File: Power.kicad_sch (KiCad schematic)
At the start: 26 parts, among them J401 KLDX-0202-B, J402 EBWA-02-B, Q401 MCU18P10Y-TP, U401 TPS7A2030PDBVR

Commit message: feat: checked REV A
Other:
- moved on the sheet: C404, C405, FID401, FID402, FID403, H401, H402, H403, H404, ID401, TP403, TP404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

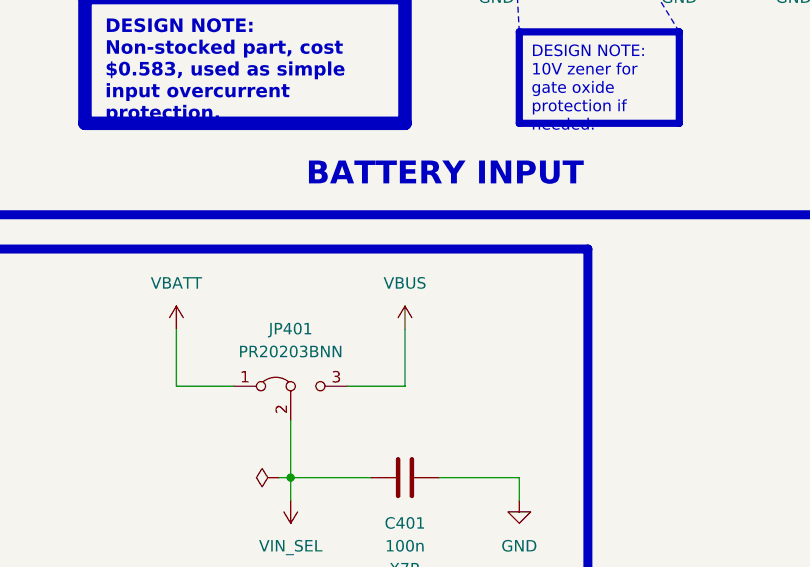
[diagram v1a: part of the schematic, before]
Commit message: fix: net naming, NC STM32 pins, silkscreen, pin 1 indicator
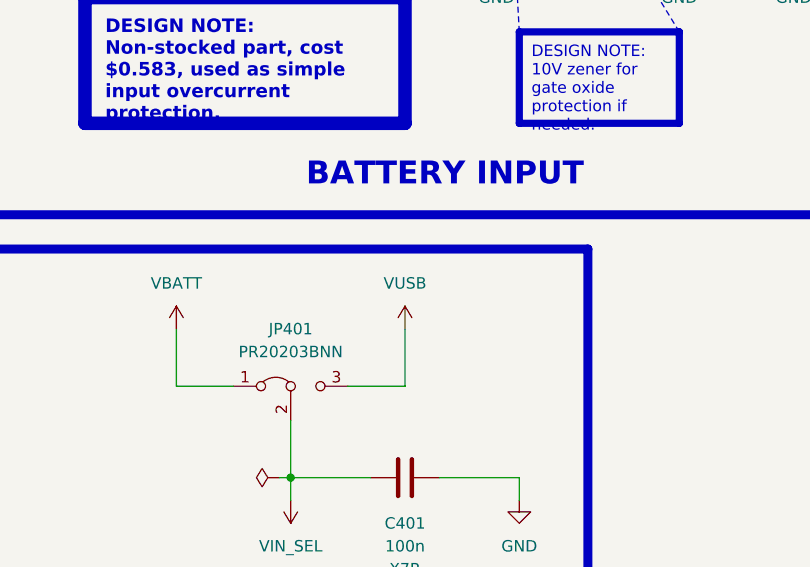
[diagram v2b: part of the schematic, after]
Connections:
- net VBUS renamed VUSB
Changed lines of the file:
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@@
 			)
 		)
-		(property "Value" "VBUS"
+		(property "Value" "VUSB"
 			(at 82.55 121.92 0)
 			(effects
@@
 			)
 		)
-		(property "Description" "Power symbol creates a global label with name \"VBUS\""
+		(property "Description" "Power symbol creates a global label with name \"VUSB\""
 			(at 82.55 127 0)
 			(effects
